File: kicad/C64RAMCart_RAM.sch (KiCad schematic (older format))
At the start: 20 parts, among them SW1 SW_SPST, U10 KM62256CLP, U11 KM62256CLP, U2 74LS74, U6 KM62256CLP, U7 KM62256CLP, U8 KM62256CLP, U9 KM62256CLP

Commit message: Gerbers and Schematic
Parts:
- added H1, H2, H3, H4: MountingHole, C64:M3_pin, symbol Mechanical:MountingHole
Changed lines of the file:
@@
 encoding utf-8
 Sheet 2 2
-Title ""
-Date ""
-Rev ""
-Comp ""
-Comment1 ""
-Comment2 ""
-Comment3 ""
-Comment4 ""
+Title "Super Luxus CMOS RAM Platine"
+Date "2023-04-19"
+Rev "Rev001"
+Comp "Redrawn by AdamT117 (kayto@github.com)"
+Comment1 "designed and created by J Schucht."
+Comment2 "The design files are offered for educational purposes only."
+Comment3 "from the 64'er magazine dated March 1989"
+Comment4 "This C64 RAM cartridge is a recreation of the Super Luxus CMOS RAM Platine"
 $EndDescr
 Wire Bus Line
@@
 Wire Wire Line
 	8925 1600 8925 1875
-Wire Bus Line
-	6825 2825 6825 3700
-Wire Bus Line
-	6825 5375 6825 6250
-Wire Bus Line
-	4650 2800 4650 3675
-Wire Bus Line
-	2400 2825 2400 3700
-Wire Bus Line
-	4650 5375 4650 6250
-Wire Bus Line
-	2400 5350 2400 6225
-Wire Bus Line
-	5075 2825 5075 4500
-Wire Bus Line
-	2900 2800 2900 4475
-Wire Bus Line
-	5075 5375 5075 7050
-Wire Bus Line
-	2900 5375 2900 7050
-Wire Bus Line
-	650  5350 650  7025
-Wire Bus Line
-	650  2825 650  4500
 Text Notes 3725 825  0    50   ~ 0
 RAM Battery Switch
+$Comp
+L Mechanical:MountingHole H1
+U 1 1 64464D83
+P 9375 2825
+F 0 "H1" H 9475 2871 50  0000 L CNN
+F 1 "MountingHole" H 9475 2780 50  0000 L CNN
+F 2 "C64:M3_pin" H 9375 2825 50  0001 C CNN
+F 3 "~" H 9375 2825 50  0001 C CNN
+	1    9375 2825
+	1    0    0    -1
+$EndComp
+$Comp
+L Mechanical:MountingHole H2
+U 1 1 644651A4
+P 9375 3225
+F 0 "H2" H 9475 3271 50  0000 L CNN
+F 1 "MountingHole" H 9475 3180 50  0000 L CNN
+F 2 "C64:M3_pin" H 9375 3225 50  0001 C CNN
+F 3 "~" H 9375 3225 50  0001 C CNN
+	1    9375 3225
+	1    0    0    -1
+$EndComp
+$Comp
+L Mechanical:MountingHole H3
+U 1 1 6447DA20
+P 9375 3625
+F 0 "H3" H 9475 3671 50  0000 L CNN
+F 1 "MountingHole" H 9475 3580 50  0000 L CNN
+F 2 "C64:M3_pin" H 9375 3625 50  0001 C CNN
+F 3 "~" H 9375 3625 50  0001 C CNN
+	1    9375 3625
+	1    0    0    -1
+$EndComp
+$Comp
+L Mechanical:MountingHole H4
+U 1 1 6447DD66
+P 9375 4025
+F 0 "H4" H 9475 4071 50  0000 L CNN
+F 1 "MountingHole" H 9475 3980 50  0000 L CNN
+F 2 "C64:M3_pin" H 9375 4025 50  0001 C CNN
+F 3 "~" H 9375 4025 50  0001 C CNN
+	1    9375 4025
+	1    0    0    -1
+$EndComp
+Wire Bus Line
+	6825 2825 6825 3700
+Wire Bus Line
+	6825 5375 6825 6250
+Wire Bus Line
+	4650 2800 4650 3675
+Wire Bus Line
+	2400 2825 2400 3700
+Wire Bus Line
+	4650 5375 4650 6250
+Wire Bus Line
+	2400 5350 2400 6225
+Wire Bus Line
+	5075 2825 5075 4500
+Wire Bus Line
+	2900 2800 2900 4475
+Wire Bus Line
+	5075 5375 5075 7050
+Wire Bus Line
+	2900 5375 2900 7050
+Wire Bus Line
+	650  5350 650  7025
+Wire Bus Line
+	650  2825 650  4500
 $EndSCHEMATC

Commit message: PCB and Schematic tidy
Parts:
- C1, C2: value C -> 100nF
- R1: value R_Small -> 390
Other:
- moved on the sheet: C1
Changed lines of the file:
@@
 	1    0    0    -1
 $EndComp
-Text GLabel 1075 1150 0    50   Input ~ 0
+Text GLabel 925  1150 0    50   Input ~ 0
 +5V
 $Comp
 L Device:C C1
 U 1 1 63E75A5D
-P 1325 1525
-F 0 "C1" H 1440 1571 50  0000 L CNN
-F 1 "C" H 1440 1480 50  0000 L CNN
-F 2 "Capacitor_THT:C_Disc_D4.3mm_W1.9mm_P5.00mm" H 1363 1375 50  0001 C CNN
-F 3 "~" H 1325 1525 50  0001 C CNN
-	1    1325 1525
+P 1175 1525
+F 0 "C1" H 1290 1571 50  0000 L CNN
+F 1 "100nF" H 1290 1480 50  0000 L CNN
+F 2 "Capacitor_THT:C_Disc_D4.3mm_W1.9mm_P5.00mm" H 1213 1375 50  0001 C CNN
+F 3 "~" H 1175 1525 50  0001 C CNN
+	1    1175 1525
 	1    0    0    -1
 $EndComp
@@
 P 1700 1525
 F 0 "C2" H 1815 1571 50  0000 L CNN
-F 1 "C" H 1815 1480 50  0000 L CNN
+F 1 "100nF" H 1815 1480 50  0000 L CNN
 F 2 "Capacitor_THT:C_Disc_D4.3mm_W1.9mm_P5.00mm" H 1738 1375 50  0001 C CNN
 F 3 "~" H 1700 1525 50  0001 C CNN
@@
 	1    0    0    -1
 $EndComp
-Text GLabel 1050 1950 0    50   Input ~ 0
+Text GLabel 900  1950 0    50   Input ~ 0
 GND
 $Comp
@@
 P 4850 850
 F 0 "R1" V 5046 850 50  0000 C CNN
-F 1 "R_Small" V 4955 850 50  0000 C CNN
+F 1 "390" V 4955 850 50  0000 C CNN
 F 2 "Resistor_THT:R_Axial_DIN0207_L6.3mm_D2.5mm_P7.62mm_Horizontal" H 4850 850 50  0001 C CNN
 F 3 "~" H 4850 850 50  0001 C CNN
@@
 	2300 1150 2650 1150
 Wire Wire Line
-	1325 1675 1325 1950
-Connection ~ 1325 1950
+	1175 1675 1175 1950
+Connection ~ 1175 1950
 Wire Wire Line
-	1325 1950 1050 1950
+	1175 1950 900  1950
 Wire Wire Line
 	1700 1675 1700 1950
 Connection ~ 1700 1950
 Wire Wire Line
-	1700 1950 1325 1950
+	1700 1950 1175 1950
 Wire Wire Line
 	1700 1375 1700 1150
 Connection ~ 1700 1150
 Wire Wire Line
-	1325 1375 1325 1150
+	1175 1375 1175 1150
 Wire Wire Line
-	1075 1150 1325 1150
-Connection ~ 1325 1150
+	925  1150 1175 1150
+Connection ~ 1175 1150
 Wire Wire Line
-	1325 1150 1700 1150
+	1175 1150 1700 1150
 Wire Wire Line
 	5175 1950 5175 1650

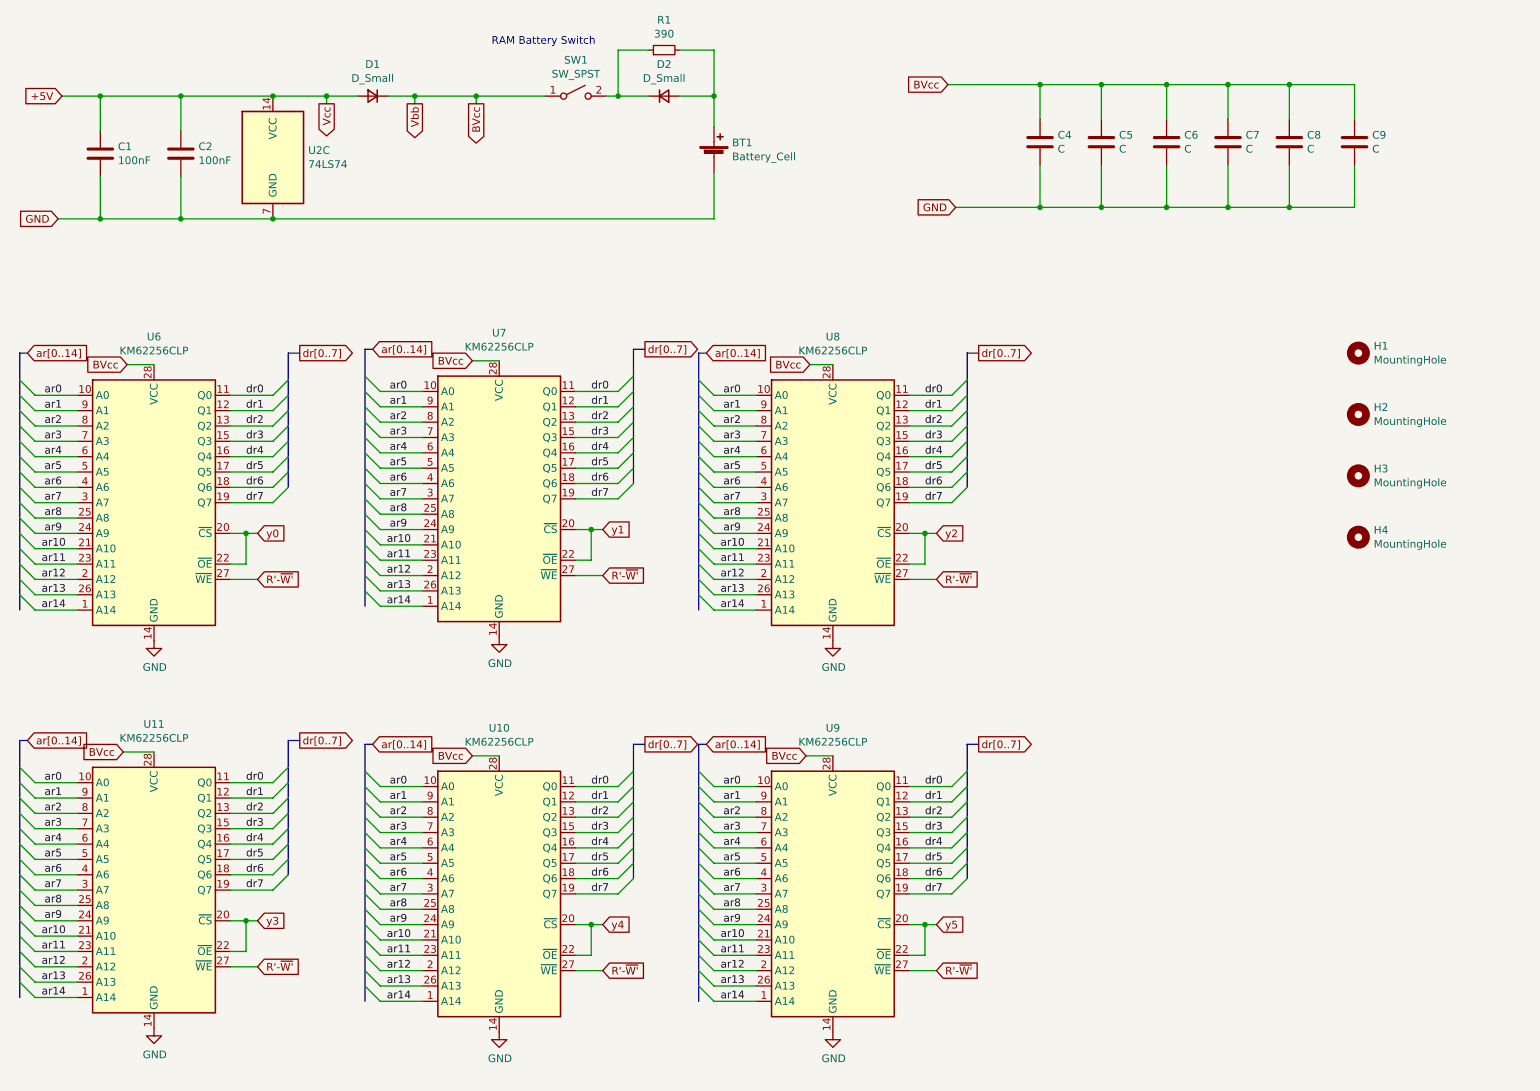
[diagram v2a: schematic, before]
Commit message: Remaining SRAM added
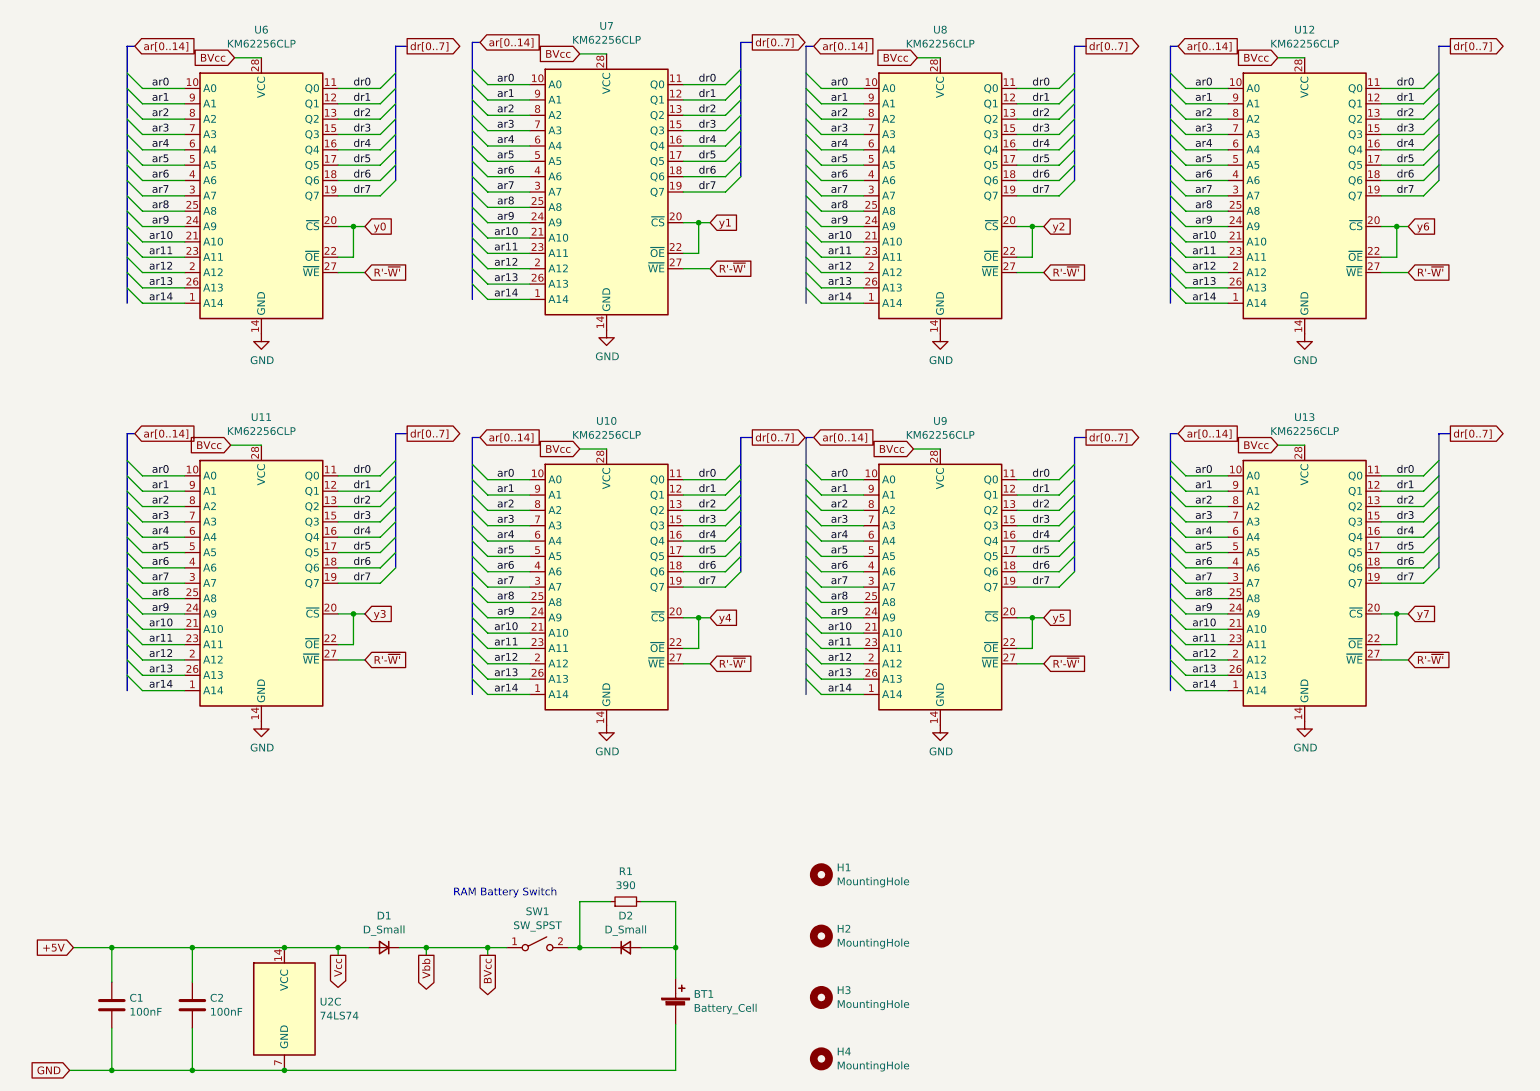
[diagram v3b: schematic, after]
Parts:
- removed C4, C5, C6, C7, C8, C9: C, Capacitor_THT:C_Disc_D4.3mm_W1.9mm_P5.00mm, symbol Device:C
- added U12, U13: KM62256CLP, Package_DIP:DIP-28_W15.24mm_Socket, symbol Memory_RAM:KM62256CLP
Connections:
- net BVcc: now also U12.28 (VCC), U13.28 (VCC)
- net GND: now also U12.14 (GND), U13.14 (GND)
- net R'-~W': now also U12.27 (~WE), U13.27 (~WE)
- net ar0: now also U12.10 (A0), U13.10 (A0)
- net ar1: now also U12.9 (A1), U13.9 (A1)
- net ar10: now also U12.21 (A10), U13.21 (A10)
- net ar11: now also U12.23 (A11), U13.23 (A11)
- net ar12: now also U12.2 (A12), U13.2 (A12)
- net ar13: now also U12.26 (A13), U13.26 (A13)
- net ar14: now also U12.1 (A14), U13.1 (A14)
- net ar2: now also U12.8 (A2), U13.8 (A2)
- net ar3: now also U12.7 (A3), U13.7 (A3)
- net ar4: now also U12.6 (A4), U13.6 (A4)
- net ar5: now also U12.5 (A5), U13.5 (A5)
- net ar6: now also U12.4 (A6), U13.4 (A6)
- net ar7: now also U12.3 (A7), U13.3 (A7)
- net ar8: now also U12.25 (A8), U13.25 (A8)
- net ar9: now also U12.24 (A9), U13.24 (A9)
- net dr0: now also U12.11 (Q0), U13.11 (Q0)
- net dr1: now also U12.12 (Q1), U13.12 (Q1)
- net dr2: now also U12.13 (Q2), U13.13 (Q2)
- net dr3: now also U12.15 (Q3), U13.15 (Q3)
- net dr4: now also U12.16 (Q4), U13.16 (Q4)
- net dr5: now also U12.17 (Q5), U13.17 (Q5)
- net dr6: now also U12.18 (Q6), U13.18 (Q6)
- net dr7: now also U12.19 (Q7), U13.19 (Q7)
- new net y6: U12.20 (~CS), U12.22 (~OE)
- new net y7: U13.20 (~CS), U13.22 (~OE)
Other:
- moved on the sheet: BT1, C1, C2, D1, D2, H1, H2, H3, H4, R1, SW1, U10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
